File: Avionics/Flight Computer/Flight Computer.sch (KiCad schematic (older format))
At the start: 4 parts

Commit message: Lots of power tree and layout work
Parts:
- added J5: 473460001, Connectors:USB_Micro-B_0473460001, symbol USB_OTG
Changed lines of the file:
@@
 LIBS:graphic
 LIBS:power
+LIBS:interface
+LIBS:linear
+LIBS:74xgxx
+LIBS:74xx
+LIBS:ac-dc
+LIBS:actel
+LIBS:adc-dac
+LIBS:allegro
+LIBS:Altera
+LIBS:analog_devices
+LIBS:analog_switches
+LIBS:Power_Management
+LIBS:powerint
 LIBS:Flight Computer-cache
-EELAYER 25 0
+EELAYER 26 0
 EELAYER END
 $Descr A4 11693 8268
@@
 $EndSheet
 $Sheet
-S 1250 1400 1400 1050
+S 1400 3400 1400 1050
 U 58AA09CD
 F0 "Power" 60
@@
 $EndComp
 $Comp
-L GND #PWR1
+L GND #PWR01
 U 1 1 58AA7E39
 P 3450 7100
-F 0 "#PWR1" H 3450 6850 50  0001 C CNN
+F 0 "#PWR01" H 3450 6850 50  0001 C CNN
 F 1 "GND" H 3450 6950 50  0000 C CNN
 F 2 "" H 3450 7100 50  0001 C CNN
@@
 $EndComp
 $Comp
-L GND #PWR2
+L GND #PWR02
 U 1 1 58AA7E55
 P 4200 7100
-F 0 "#PWR2" H 4200 6850 50  0001 C CNN
+F 0 "#PWR02" H 4200 6850 50  0001 C CNN
 F 1 "GND" H 4200 6950 50  0000 C CNN
 F 2 "" H 4200 7100 50  0001 C CNN
@@
 $EndComp
 $Comp
-L GND #PWR3
+L GND #PWR03
 U 1 1 58AA7E71
 P 4950 7100
-F 0 "#PWR3" H 4950 6850 50  0001 C CNN
+F 0 "#PWR03" H 4950 6850 50  0001 C CNN
 F 1 "GND" H 4950 6950 50  0000 C CNN
 F 2 "" H 4950 7100 50  0001 C CNN
@@
 $EndComp
 $Comp
-L GND #PWR4
+L GND #PWR04
 U 1 1 58AA7E8D
 P 5700 7100
-F 0 "#PWR4" H 5700 6850 50  0001 C CNN
+F 0 "#PWR04" H 5700 6850 50  0001 C CNN
 F 1 "GND" H 5700 6950 50  0000 C CNN
 F 2 "" H 5700 7100 50  0001 C CNN
@@
 	1    0    0    -1
 $EndComp
+$Comp
+L USB_OTG J5
+U 1 1 58AB5F89
+P 1950 2000
+F 0 "J5" H 2005 2467 50  0000 C CNN
+F 1 "473460001" H 2005 2376 50  0000 C CNN
+F 2 "Connectors:USB_Micro-B_0473460001" H -7600 -1300 50  0001 C CNN
+F 3 "http://www.molex.com/pdm_docs/sd/473460001_sd.pdf" H -7600 -1300 50  0001 C CNN
+	1    1950 2000
+	1    0    0    -1
+$EndComp

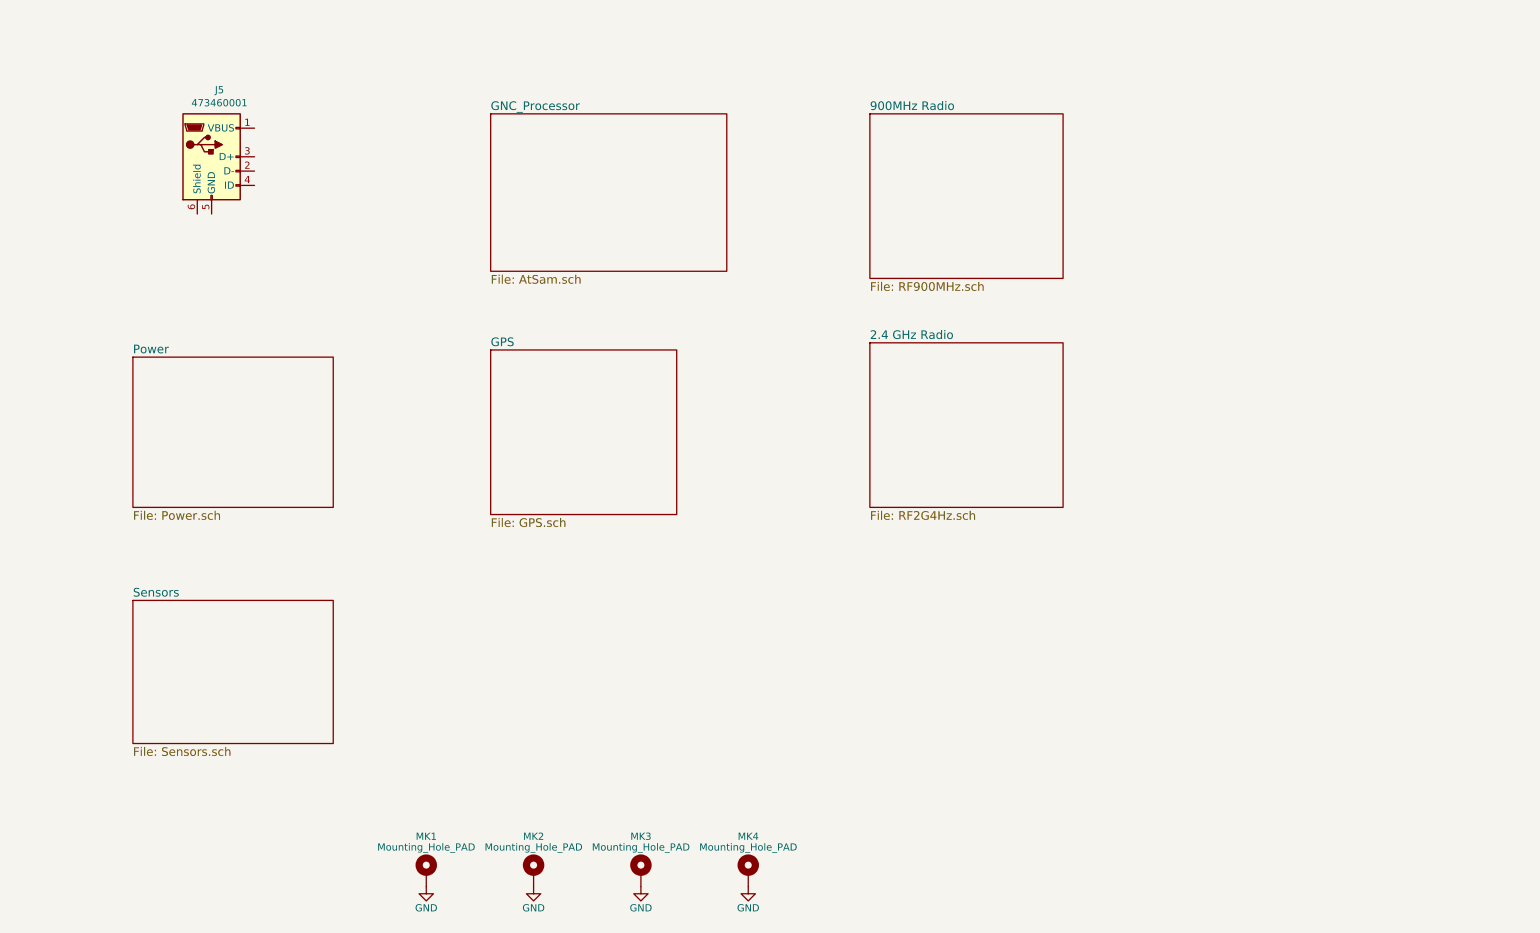
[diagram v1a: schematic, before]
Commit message: Restarted initial layout and cleaned up decoupling/RF layout.
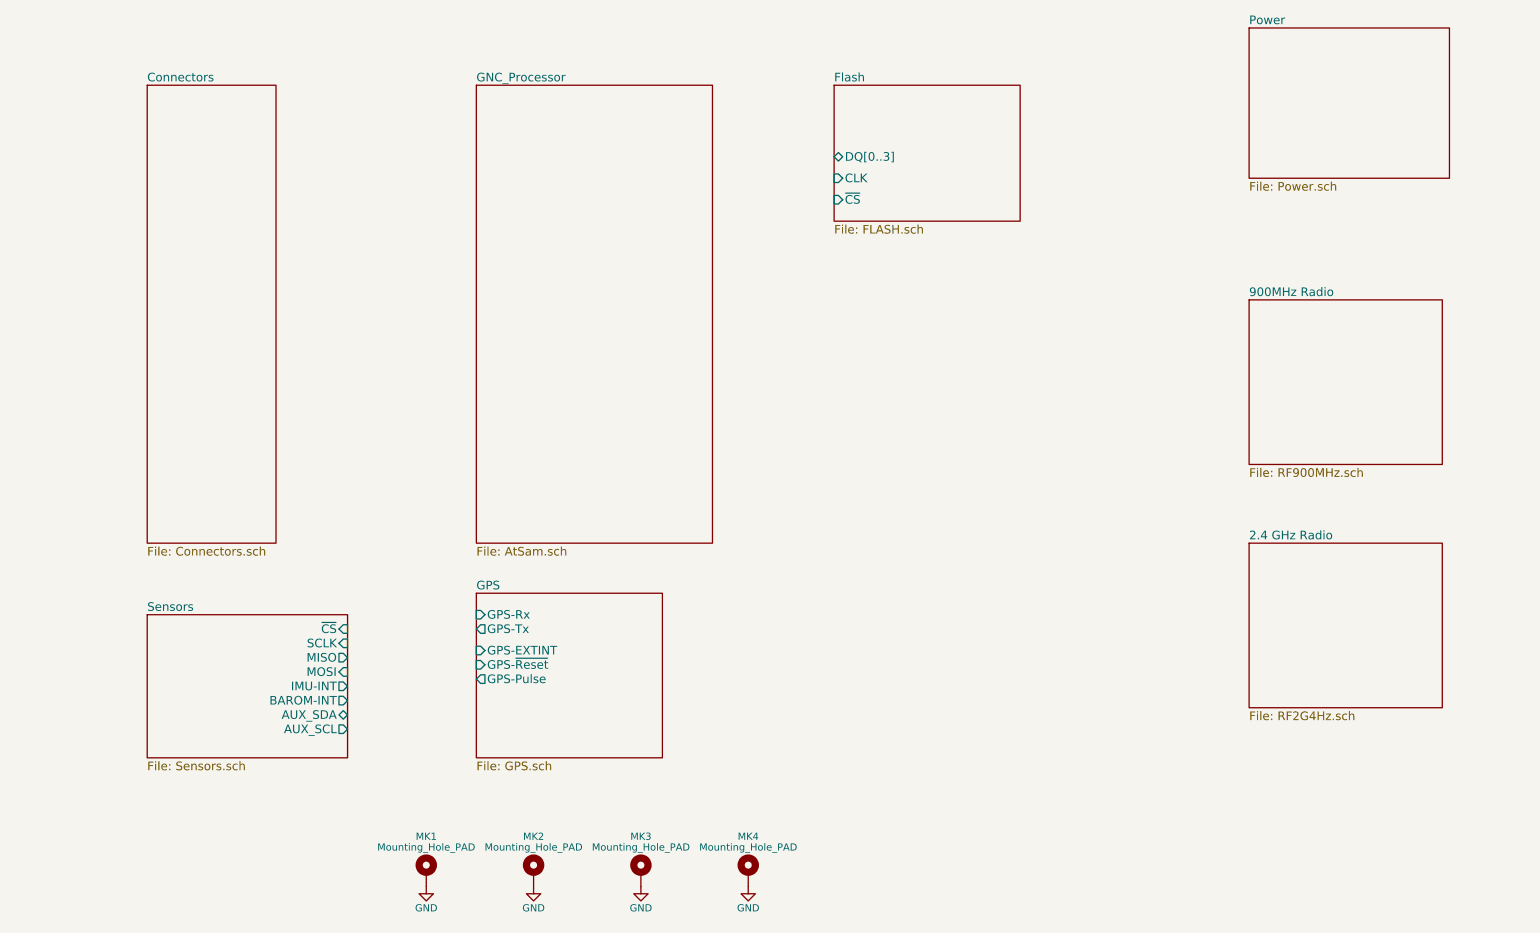
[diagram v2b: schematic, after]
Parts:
- removed J5: 473460001, Connectors:USB_Micro-B_0473460001, symbol USB_OTG
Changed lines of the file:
@@
 EESchema Schematic File Version 2
+LIBS:Flight Computer-rescue
 LIBS:device
 LIBS:rfcom
@@
 $Descr A4 11693 8268
 encoding utf-8
-Sheet 1 7
+Sheet 1 9
 Title ""
 Date ""
@@
 $EndDescr
 $Sheet
-S 3900 1700 1650 1100
+S 3800 1500 1650 3200
 U 58AA09BD
 F0 "GNC_Processor" 60
@@
 $EndSheet
 $Sheet
-S 6550 1700 1350 1150
+S 9200 3000 1350 1150
 U 58AA09C2
 F0 "900MHz Radio" 60
@@
 $EndSheet
 $Sheet
-S 6550 3300 1350 1150
+S 9200 4700 1350 1150
 U 58AA09C5
 F0 "2.4 GHz Radio" 60
@@
 $EndSheet
 $Sheet
-S 3900 3350 1300 1150
+S 3800 5050 1300 1150
 U 58AA09C8
 F0 "GPS" 60
 F1 "GPS.sch" 60
+F2 "GPS-Rx" I L 3800 5200 60
+F3 "GPS-Tx" O L 3800 5300 60
+F4 "GPS-EXTINT" I L 3800 5450 60
+F5 "GPS-~Reset" I L 3800 5550 60
+F6 "GPS-Pulse" O L 3800 5650 60
 $EndSheet
 $Sheet
-S 1400 3400 1400 1050
+S 9200 1100 1400 1050
 U 58AA09CD
 F0 "Power" 60
@@
 $EndSheet
 $Sheet
-S 1400 5100 1400 1000
+S 1500 5200 1400 1000
 U 58AA09D0
 F0 "Sensors" 60
 F1 "Sensors.sch" 60
+F2 "~CS" I R 2900 5300 60
+F3 "SCLK" I R 2900 5400 60
+F4 "MISO" O R 2900 5500 60
+F5 "MOSI" I R 2900 5600 60
+F6 "IMU-INT" O R 2900 5700 60
+F7 "BAROM-INT" O R 2900 5800 60
+F8 "AUX_SDA" B R 2900 5900 60
+F9 "AUX_SCL" O R 2900 6000 60
 $EndSheet
 $Comp
@@
 	1    0    0    -1
 $EndComp
-$Comp
-L USB_OTG J5
-U 1 1 58AB5F89
-P 1950 2000
-F 0 "J5" H 2005 2467 50  0000 C CNN
-F 1 "473460001" H 2005 2376 50  0000 C CNN
-F 2 "Connectors:USB_Micro-B_0473460001" H -7600 -1300 50  0001 C CNN
-F 3 "http://www.molex.com/pdm_docs/sd/473460001_sd.pdf" H -7600 -1300 50  0001 C CNN
-	1    1950 2000
-	1    0    0    -1
-$EndComp
+$Sheet
+S 6300 1500 1300 950
+U 58B11274
+F0 "Flash" 60
+F1 "FLASH.sch" 60
+F2 "~CS" I L 6300 2300 60
+F3 "CLK" I L 6300 2150 60
+F4 "DQ[0..3]" B L 6300 2000 60
+$EndSheet
+$Sheet
+S 1500 1500 900  3200
+U 58B5360A
+F0 "Connectors" 60
+F1 "Connectors.sch" 60
+$EndSheet
 $EndSCHEMATC

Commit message: Nearly completed initial placement.
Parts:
- removed MK2, MK4: Mounting_Hole_PAD, Mounting_Holes:MountingHole_3mm_Pad_Via, symbol Mounting_Hole_PAD
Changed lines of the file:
@@
 F0 "GNC_Processor" 60
 F1 "AtSam.sch" 60
+F2 "QIO[0..3]" B R 5450 1600 60
+F3 "QSCK" O R 5450 1700 60
+F4 "QCS" O R 5450 1800 60
+F5 "USBD_N" B L 3800 1700 60
+F6 "USBD_P" B L 3800 1600 60
 $EndSheet
 $Sheet
@@
 $EndSheet
 $Comp
-L Mounting_Hole_PAD MK2
-U 1 1 58AA7AFA
-P 4200 7000
-F 0 "MK2" H 4200 7250 50  0000 C CNN
-F 1 "Mounting_Hole_PAD" H 4200 7175 50  0000 C CNN
-F 2 "Mounting_Holes:MountingHole_3mm_Pad_Via" H 4200 7000 50  0001 C CNN
-F 3 "" H 4200 7000 50  0001 C CNN
-	1    4200 7000
-	1    0    0    -1
-$EndComp
-$Comp
 L Mounting_Hole_PAD MK3
 U 1 1 58AA7D1A
@@
 $EndComp
 $Comp
-L Mounting_Hole_PAD MK4
-U 1 1 58AA7DF7
-P 5700 7000
-F 0 "MK4" H 5700 7250 50  0000 C CNN
-F 1 "Mounting_Hole_PAD" H 5700 7175 50  0000 C CNN
-F 2 "Mounting_Holes:MountingHole_3mm_Pad_Via" H 5700 7000 50  0001 C CNN
-F 3 "" H 5700 7000 50  0001 C CNN
-	1    5700 7000
-	1    0    0    -1
-$EndComp
-$Comp
 L GND #PWR01
 U 1 1 58AA7E39
@@
 $Comp
 L GND #PWR02
-U 1 1 58AA7E55
-P 4200 7100
-F 0 "#PWR02" H 4200 6850 50  0001 C CNN
-F 1 "GND" H 4200 6950 50  0000 C CNN
-F 2 "" H 4200 7100 50  0001 C CNN
-F 3 "" H 4200 7100 50  0001 C CNN
-	1    4200 7100
-	1    0    0    -1
-$EndComp
-$Comp
-L GND #PWR03
 U 1 1 58AA7E71
 P 4950 7100
-F 0 "#PWR03" H 4950 6850 50  0001 C CNN
+F 0 "#PWR02" H 4950 6850 50  0001 C CNN
 F 1 "GND" H 4950 6950 50  0000 C CNN
 F 2 "" H 4950 7100 50  0001 C CNN
@@
 	1    0    0    -1
 $EndComp
-$Comp
-L GND #PWR04
-U 1 1 58AA7E8D
-P 5700 7100
-F 0 "#PWR04" H 5700 6850 50  0001 C CNN
-F 1 "GND" H 5700 6950 50  0000 C CNN
-F 2 "" H 5700 7100 50  0001 C CNN
-F 3 "" H 5700 7100 50  0001 C CNN
-	1    5700 7100
-	1    0    0    -1
-$EndComp
 $Sheet
-S 6300 1500 1300 950
+S 5750 1500 600  400
 U 58B11274
 F0 "Flash" 60
 F1 "FLASH.sch" 60
-F2 "~CS" I L 6300 2300 60
-F3 "CLK" I L 6300 2150 60
-F4 "DQ[0..3]" B L 6300 2000 60
+F2 "~CS" I L 5750 1800 60
+F3 "CLK" I L 5750 1700 60
+F4 "DQ[0..3]" B L 5750 1600 60
 $EndSheet
 $Sheet
@@
 F0 "Connectors" 60
 F1 "Connectors.sch" 60
+F2 "USBD_P" B R 2400 1600 60
+F3 "USBD_N" B R 2400 1700 60
 $EndSheet
+Wire Bus Line
+	5450 1600 5750 1600
+Wire Wire Line
+	5450 1700 5750 1700
+Wire Wire Line
+	5450 1800 5750 1800
+Wire Wire Line
+	3800 1600 2400 1600
+Wire Wire Line
+	2400 1700 3800 1700
 $EndSCHEMATC

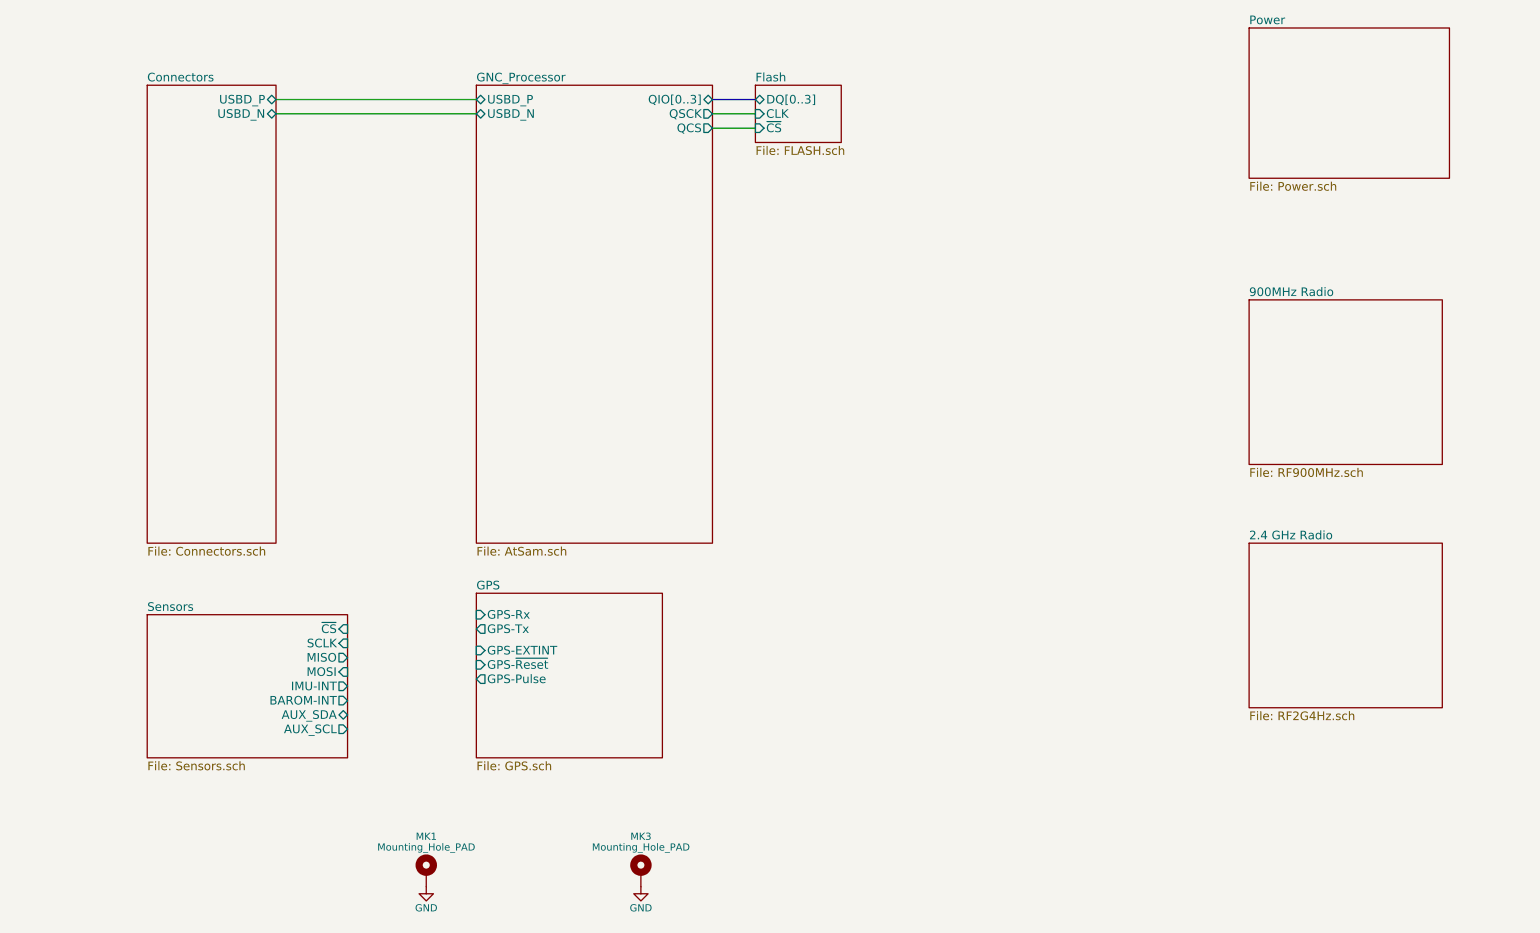
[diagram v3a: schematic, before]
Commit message: Added additional pinout
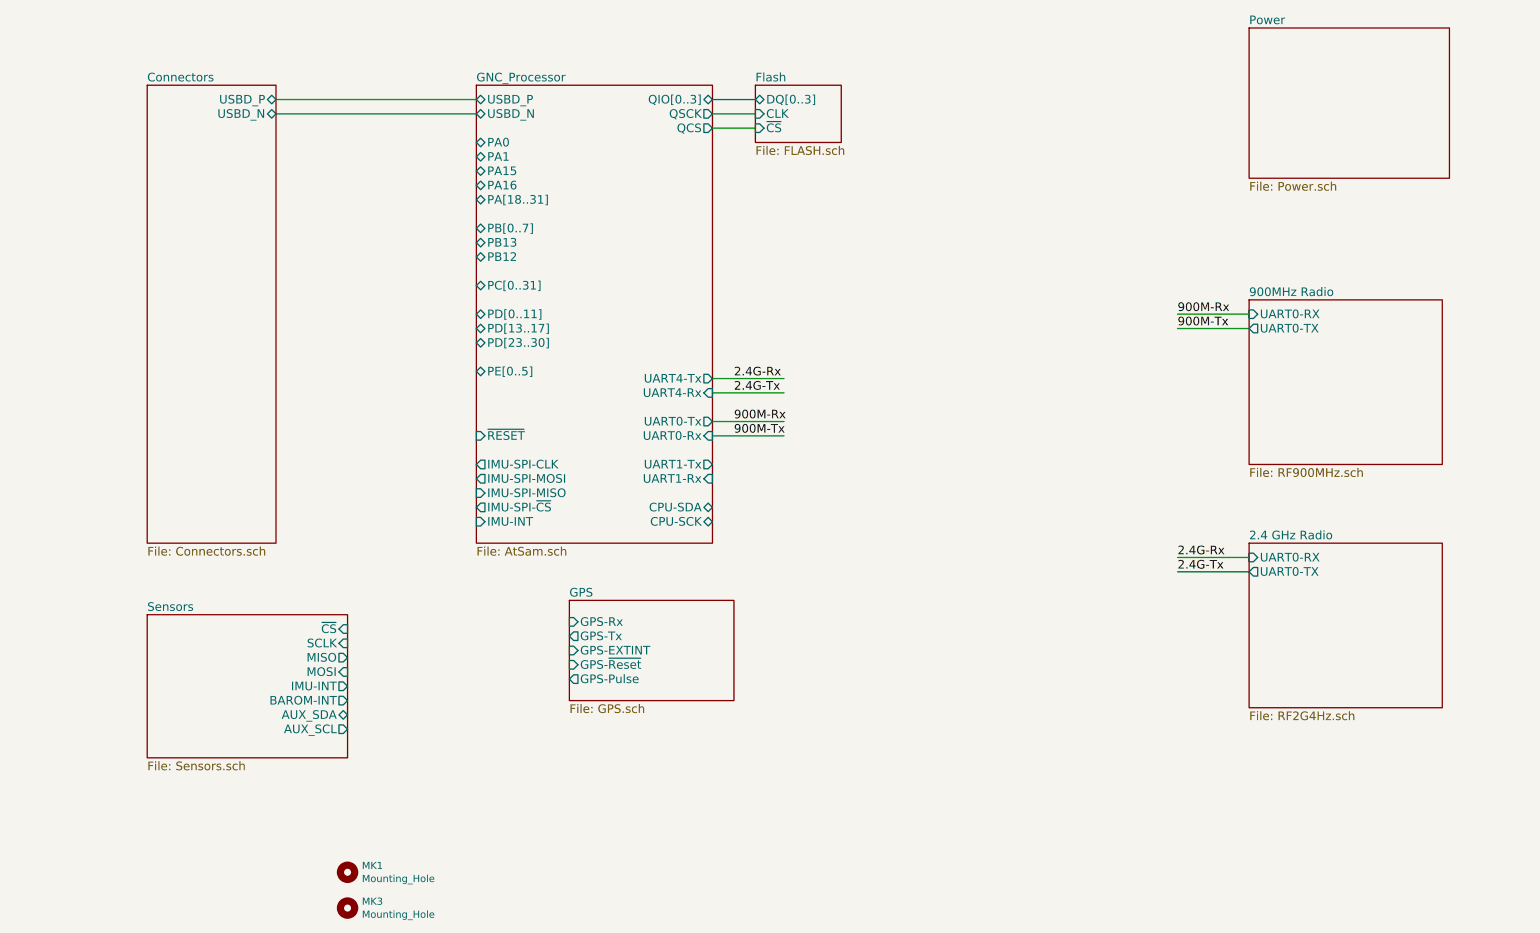
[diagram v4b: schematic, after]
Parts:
- removed MK1, MK3: Mounting_Hole_PAD, Mounting_Holes:MountingHole_3mm_Pad_Via, symbol Mounting_Hole_PAD
- added MK1, MK3: Mounting_Hole, Mounting_Holes:MountingHole_2.5mm, symbol Mounting_Hole
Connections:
- net labels added: 2.4G-Rx, 2.4G-Tx, 900M-Rx, 900M-Tx
- net labels removed: GND
- wire segments 4 -> 12
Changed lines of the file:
@@
 F5 "USBD_N" B L 3800 1700 60
 F6 "USBD_P" B L 3800 1600 60
+F7 "PA0" B L 3800 1900 60
+F8 "PA1" B L 3800 2000 60
+F9 "PA15" B L 3800 2100 60
+F10 "PA16" B L 3800 2200 60
+F11 "PA[18..31]" B L 3800 2300 60
+F12 "IMU-INT" I L 3800 4550 60
+F13 "CPU-SDA" B R 5450 4450 60
+F14 "CPU-SCK" B R 5450 4550 60
+F15 "UART1-Rx" I R 5450 4250 60
+F16 "UART1-Tx" O R 5450 4150 60
+F17 "UART0-Tx" O R 5450 3850 60
+F18 "UART0-Rx" I R 5450 3950 60
+F19 "~RESET" I L 3800 3950 60
+F20 "PB[0..7]" B L 3800 2500 60
+F21 "PB13" B L 3800 2600 60
+F22 "PB12" B L 3800 2700 60
+F23 "PC[0..31]" B L 3800 2900 60
+F24 "UART4-Rx" I R 5450 3650 60
+F25 "UART4-Tx" O R 5450 3550 60
+F26 "IMU-SPI-~CS" O L 3800 4450 60
+F27 "IMU-SPI-MISO" I L 3800 4350 60
+F28 "IMU-SPI-MOSI" O L 3800 4250 60
+F29 "IMU-SPI-CLK" O L 3800 4150 60
+F30 "PD[0..11]" B L 3800 3100 60
+F31 "PD[13..17]" B L 3800 3200 60
+F32 "PD[23..30]" B L 3800 3300 60
+F33 "PE[0..5]" B L 3800 3500 60
 $EndSheet
 $Sheet
@@
 F0 "900MHz Radio" 60
 F1 "RF900MHz.sch" 60
+F2 "UART0-RX" I L 9200 3100 60
+F3 "UART0-TX" O L 9200 3200 60
 $EndSheet
 $Sheet
@@
 F0 "2.4 GHz Radio" 60
 F1 "RF2G4Hz.sch" 60
+F2 "UART0-RX" I L 9200 4800 60
+F3 "UART0-TX" O L 9200 4900 60
 $EndSheet
 $Sheet
-S 3800 5050 1300 1150
+S 4450 5100 1150 700
 U 58AA09C8
 F0 "GPS" 60
 F1 "GPS.sch" 60
-F2 "GPS-Rx" I L 3800 5200 60
-F3 "GPS-Tx" O L 3800 5300 60
-F4 "GPS-EXTINT" I L 3800 5450 60
-F5 "GPS-~Reset" I L 3800 5550 60
-F6 "GPS-Pulse" O L 3800 5650 60
+F2 "GPS-Rx" I L 4450 5250 60
+F3 "GPS-Tx" O L 4450 5350 60
+F4 "GPS-EXTINT" I L 4450 5450 60
+F5 "GPS-~Reset" I L 4450 5550 60
+F6 "GPS-Pulse" O L 4450 5650 60
 $EndSheet
 $Sheet
@@
 F9 "AUX_SCL" O R 2900 6000 60
 $EndSheet
-$Comp
-L Mounting_Hole_PAD MK3
-U 1 1 58AA7D1A
-P 4950 7000
-F 0 "MK3" H 4950 7250 50  0000 C CNN
-F 1 "Mounting_Hole_PAD" H 4950 7175 50  0000 C CNN
-F 2 "Mounting_Holes:MountingHole_3mm_Pad_Via" H 4950 7000 50  0001 C CNN
-F 3 "" H 4950 7000 50  0001 C CNN
-	1    4950 7000
-	1    0    0    -1
-$EndComp
-$Comp
-L Mounting_Hole_PAD MK1
-U 1 1 58AA7DBC
-P 3450 7000
-F 0 "MK1" H 3450 7250 50  0000 C CNN
-F 1 "Mounting_Hole_PAD" H 3450 7175 50  0000 C CNN
-F 2 "Mounting_Holes:MountingHole_3mm_Pad_Via" H 3450 7000 50  0001 C CNN
-F 3 "" H 3450 7000 50  0001 C CNN
-	1    3450 7000
-	1    0    0    -1
-$EndComp
-$Comp
-L GND #PWR01
-U 1 1 58AA7E39
-P 3450 7100
-F 0 "#PWR01" H 3450 6850 50  0001 C CNN
-F 1 "GND" H 3450 6950 50  0000 C CNN
-F 2 "" H 3450 7100 50  0001 C CNN
-F 3 "" H 3450 7100 50  0001 C CNN
-	1    3450 7100
-	1    0    0    -1
-$EndComp
-$Comp
-L GND #PWR02
-U 1 1 58AA7E71
-P 4950 7100
-F 0 "#PWR02" H 4950 6850 50  0001 C CNN
-F 1 "GND" H 4950 6950 50  0000 C CNN
-F 2 "" H 4950 7100 50  0001 C CNN
-F 3 "" H 4950 7100 50  0001 C CNN
-	1    4950 7100
-	1    0    0    -1
-$EndComp
 $Sheet
 S 5750 1500 600  400
@@
 F3 "USBD_N" B R 2400 1700 60
 $EndSheet
+Text Label 5600 3550 0    60   ~ 0
+2.4G-Rx
+Text Label 5600 3650 0    60   ~ 0
+2.4G-Tx
+Text Label 8700 4800 0    60   ~ 0
+2.4G-Rx
+Text Label 8700 4900 0    60   ~ 0
+2.4G-Tx
 Wire Bus Line
 	5450 1600 5750 1600
@@
 Wire Wire Line
 	2400 1700 3800 1700
+Wire Wire Line
+	9200 4800 8700 4800
+Wire Wire Line
+	8700 4900 9200 4900
+Wire Wire Line
+	5450 3550 5950 3550
+Wire Wire Line
+	5450 3650 5950 3650
+Text Label 8700 3100 0    60   ~ 0
+900M-Rx
+Text Label 8700 3200 0    60   ~ 0
+900M-Tx
+Wire Wire Line
+	9200 3100 8700 3100
+Wire Wire Line
+	8700 3200 9200 3200
+Text Label 5600 3850 0    60   ~ 0
+900M-Rx
+Text Label 5600 3950 0    60   ~ 0
+900M-Tx
+Wire Wire Line
+	5950 3850 5450 3850
+Wire Wire Line
+	5450 3950 5950 3950
+$Comp
+L Mounting_Hole MK1
+U 1 1 58BDD655
+P 2900 7000
+F 0 "MK1" H 3000 7046 50  0000 L CNN
+F 1 "Mounting_Hole" H 3000 6955 50  0000 L CNN
+F 2 "Mounting_Holes:MountingHole_2.5mm" H -1300 -50 50  0001 C CNN
+F 3 "" H -1300 -50 50  0001 C CNN
+	1    2900 7000
+	1    0    0    -1
+$EndComp
+$Comp
+L Mounting_Hole MK3
+U 1 1 58BDE299
+P 2900 7250
+F 0 "MK3" H 3000 7296 50  0000 L CNN
+F 1 "Mounting_Hole" H 3000 7205 50  0000 L CNN
+F 2 "Mounting_Holes:MountingHole_2.5mm" H -1300 200 50  0001 C CNN
+F 3 "" H -1300 200 50  0001 C CNN
+	1    2900 7250
+	1    0    0    -1
+$EndComp
 $EndSCHEMATC
